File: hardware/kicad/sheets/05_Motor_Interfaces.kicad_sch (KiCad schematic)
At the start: 0 parts

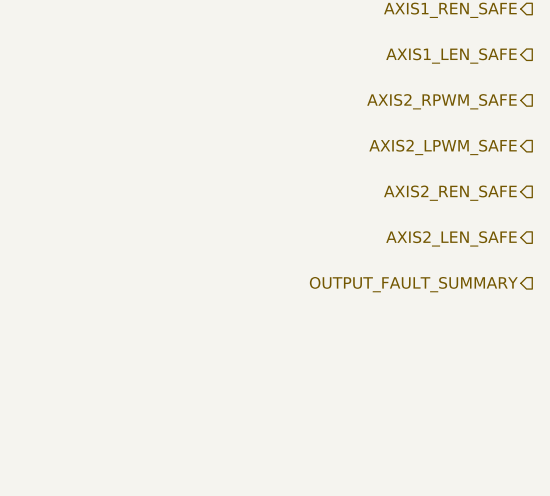
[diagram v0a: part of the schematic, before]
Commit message: Resolve Rev A motion interface contract
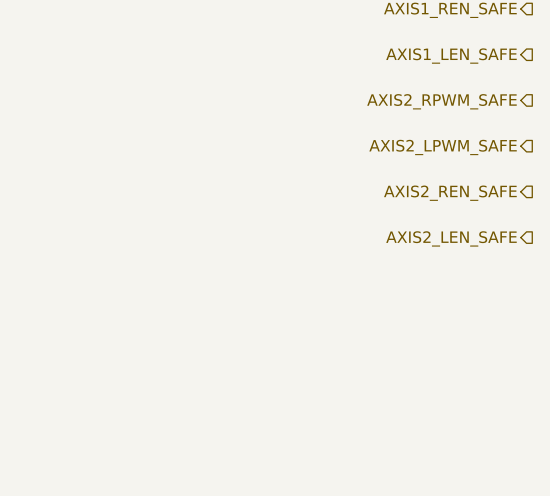
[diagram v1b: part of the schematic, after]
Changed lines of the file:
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@@
-    (effects (font (size 1.27 1.27)) (justify right))
-  )
-  (hierarchical_label "OUTPUT_FAULT_SUMMARY" (shape output) (at 180 85.64 180)
     (effects (font (size 1.27 1.27)) (justify right))
   )

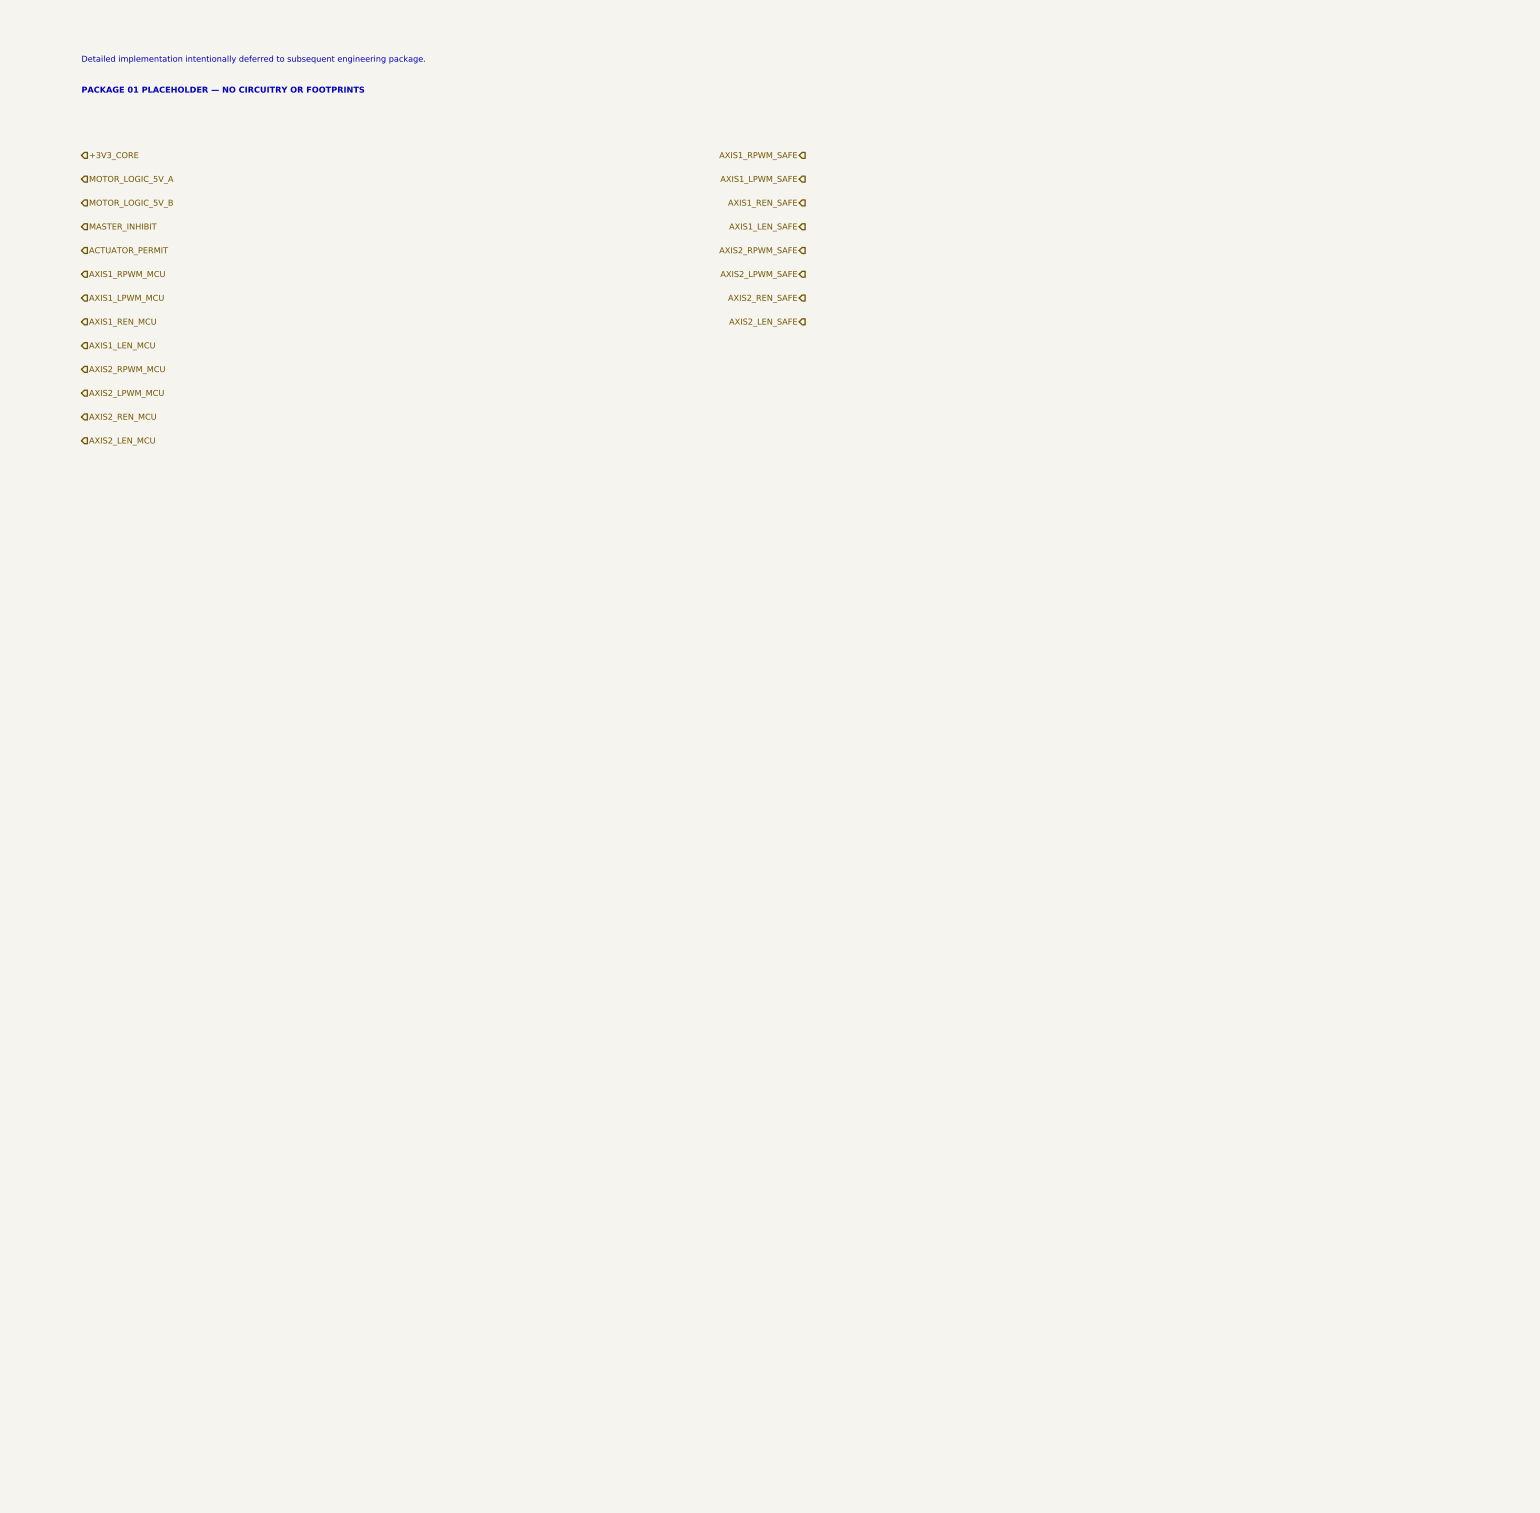
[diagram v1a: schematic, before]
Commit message: Implement dual-axis motion interface
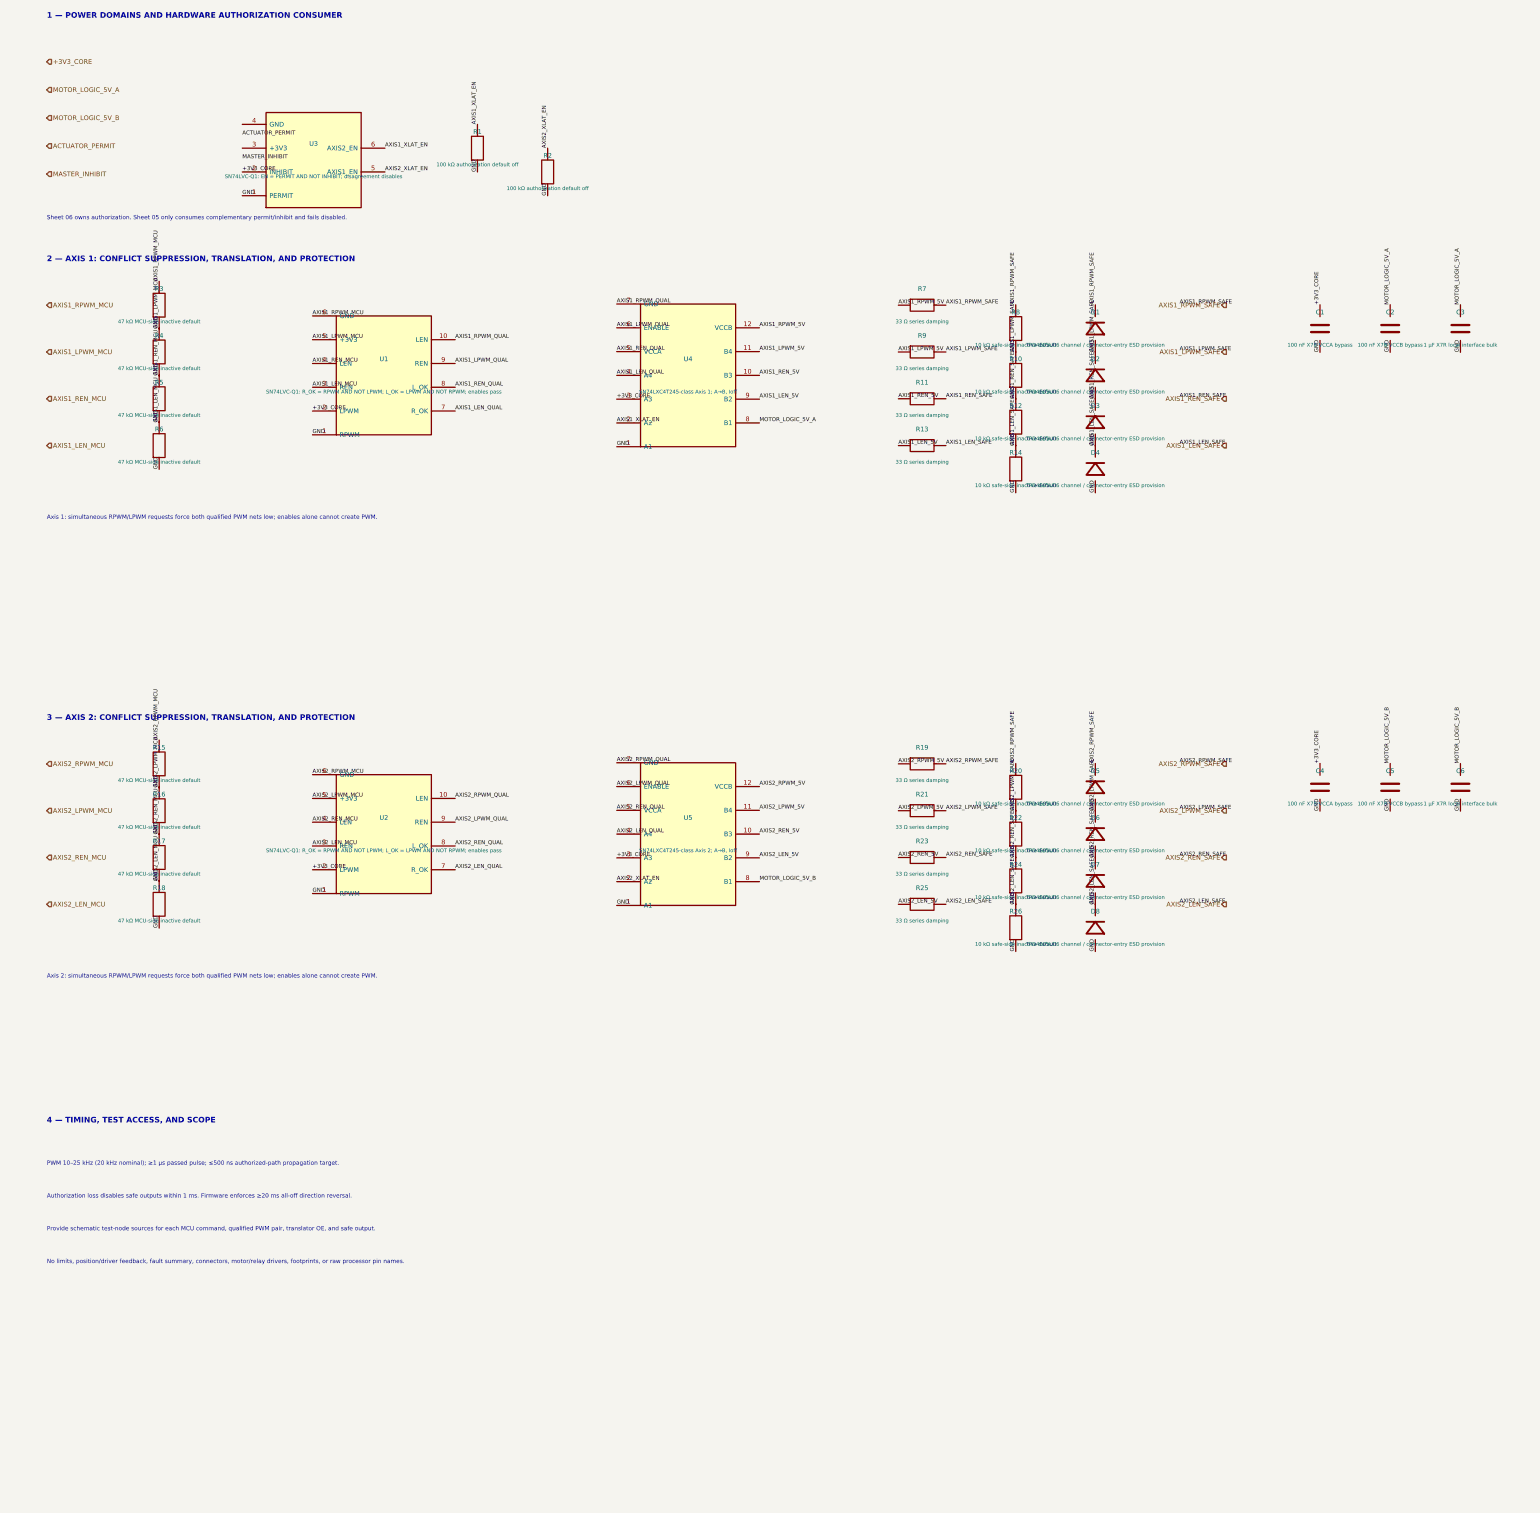
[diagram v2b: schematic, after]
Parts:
- added C1, C4: 100 nF X7R VCCA bypass, symbol IPC100:C
- added C2, C5: 100 nF X7R VCCB bypass, symbol IPC100:C
- added C3, C6: 1 µF X7R local interface bulk, symbol IPC100:C
- added D1, D2, D3, D4, D5, D6, D7, D8: TPD4E05U06 channel / connector-entry ESD provision, symbol IPC100:D
- added R1, R2: 100 kΩ authorization default off, symbol IPC100:R
- added R10, R12, R14, R20, R22, R24, R26, R8: 10 kΩ safe-side inactive default, symbol IPC100:R
- added R11, R13, R19, R21, R23, R25, R7, R9: 33 Ω series damping, symbol IPC100:R
- added R15, R16, R17, R18, R3, R4, R5, R6: 47 kΩ MCU-side inactive default, symbol IPC100:R
- added U1, U2: SN74LVC-Q1: R_OK = RPWM AND NOT LPWM; L_OK = LPWM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, symbol IPC100:INTERLOCK4
- added U3: SN74LVC-Q1: EN = PERMIT AND NOT INHIBIT; disagree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, symbol IPC100:AUTH2
- added U4: SN74LXC4T245-class Axis 1; A→B, Ioff, symbol IPC100:XLAT4
- added U5: SN74LXC4T245-class Axis 2; A→B, Ioff, symbol IPC100:XLAT4
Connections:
- net +3V3_CORE: now also C1.2, C4.2, U1.2 (LPWM), U2.2 (LPWM), U3.2 (INHIBIT), U4.3 (A3), U5.3 (A3)
- net AXIS1_LEN_MCU: now also R6.2, U1.3 (REN)
- net AXIS1_LEN_SAFE: now also D4.2, R13.2, R14.2
- net AXIS1_LPWM_MCU: now also R4.2, U1.5 (+3V3)
- net AXIS1_LPWM_SAFE: now also D2.2, R10.2, R9.2
- net AXIS1_REN_MCU: now also R5.2, U1.4 (LEN)
- net AXIS1_REN_SAFE: now also D3.2, R11.2, R12.2
- net AXIS1_RPWM_MCU: now also R3.2, U1.6 (GND)
- net AXIS1_RPWM_SAFE: now also D1.2, R7.2, R8.2
- net AXIS2_LEN_MCU: now also R18.2, U2.3 (REN)
- net AXIS2_LEN_SAFE: now also D8.2, R25.2, R26.2
- net AXIS2_LPWM_MCU: now also R16.2, U2.5 (+3V3)
- net AXIS2_LPWM_SAFE: now also D6.2, R21.2, R22.2
- net AXIS2_REN_MCU: now also R17.2, U2.4 (LEN)
- net AXIS2_REN_SAFE: now also D7.2, R23.2, R24.2
- net AXIS2_RPWM_MCU: now also R15.2, U2.6 (GND)
- net AXIS2_RPWM_SAFE: now also D5.2, R19.2, R20.2
- net MOTOR_LOGIC_5V_A: now also C2.2, C3.2, U4.8 (B1)
- net MOTOR_LOGIC_5V_B: now also C5.2, C6.2, U5.8 (B1)
- new net AXIS1_LEN_5V: R13.1, U4.9 (B2)
- new net AXIS1_LEN_QUAL: U1.7 (R_OK), U4.4 (A4)
- new net AXIS1_LPWM_5V: R9.1, U4.11 (B4)
- new net AXIS1_LPWM_QUAL: U1.9 (REN), U4.6 (ENABLE)
- new net AXIS1_REN_5V: R11.1, U4.10 (B3)
- new net AXIS1_REN_QUAL: U1.8 (L_OK), U4.5 (VCCA)
- new net AXIS1_RPWM_5V: R7.1, U4.12 (VCCB)
- new net AXIS1_RPWM_QUAL: U1.10 (LEN), U4.7 (GND)
- new net AXIS1_XLAT_EN: R1.2, U3.6 (AXIS2_EN), U4.2 (A2)
- new net AXIS2_LEN_5V: R25.1, U5.9 (B2)
- new net AXIS2_LEN_QUAL: U2.7 (R_OK), U5.4 (A4)
- new net AXIS2_LPWM_5V: R21.1, U5.11 (B4)
- new net AXIS2_LPWM_QUAL: U2.9 (REN), U5.6 (ENABLE)
- new net AXIS2_REN_5V: R23.1, U5.10 (B3)
- new net AXIS2_REN_QUAL: U2.8 (L_OK), U5.5 (VCCA)
- new net AXIS2_RPWM_5V: R19.1, U5.12 (VCCB)
- new net AXIS2_RPWM_QUAL: U2.10 (LEN), U5.7 (GND)
- new net AXIS2_XLAT_EN: R2.2, U3.5 (AXIS1_EN), U5.2 (A2)
- new net GND: C1.1, C2.1, C3.1, C4.1, C5.1, C6.1, D1.1, D2.1, D3.1, D4.1, D5.1, D6.1, D7.1, D8.1, R1.1, R10.1, R12.1, R14.1, R15.1, R16.1, R17.1, R18.1, R2.1, R20.1, R22.1, R24.1, R26.1, R3.1, R4.1, R5.1, R6.1, R8.1, U1.1 (RPWM), U2.1 (RPWM), U3.1 (PERMIT), U4.1 (A1), U5.1 (A1)
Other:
- note added: "1 — POWER DOMAINS AND HARDWARE AUTHORIZATION CONSUMER"
- note added: "2 — AXIS 1: CONFLICT SUPPRESSION, TRANSLATION, AND PROTECTION"
- note added: "3 — AXIS 2: CONFLICT SUPPRESSION, TRANSLATION, AND PROTECTION"
- note added: "4 — TIMING, TEST ACCESS, AND SCOPE"
- note added: "Authorization loss disables safe outputs within 1 ms. Firmware enforces ≥20 ms all-off direction reversal."
- note added: "Axis 1: simultaneous RPWM/LPWM requests force both qualified PWM nets low; enables alone cannot create PWM."
- note added: "Axis 2: simultaneous RPWM/LPWM requests force both qualified PWM nets low; enables alone cannot create PWM."
- note added: "No limits, position/driver feedback, fault summary, connectors, motor/relay drivers, footprints, or raw processor pin names."
- note added: "PWM 10–25 kHz (20 kHz nominal); ≥1 µs passed pulse; ≤500 ns authorized-path propagation target."
- note added: "Provide schematic test-node sources for each MCU command, qualified PWM pair, translator OE, and safe output."
- note added: "Sheet 06 owns authorization. Sheet 05 only consumes complementary permit/inhibit and fails disabled."
- note removed: "Detailed implementation intentionally deferred to subsequent engineering package."
- note removed: "PACKAGE 01 PLACEHOLDER — NO CIRCUITRY OR FOOTPRINTS"
- title: IPC-100 Rev A — 05 Motor Interfaces -> IPC-100 Rev A — 05 Axis Command Interface

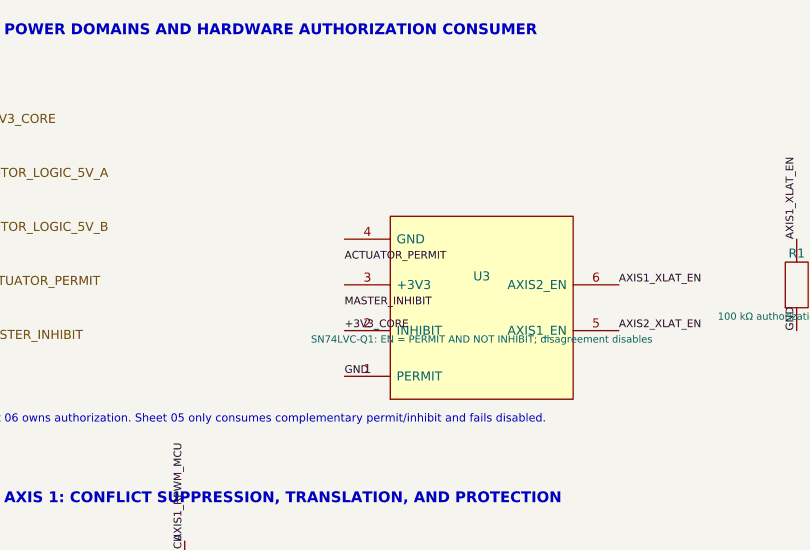
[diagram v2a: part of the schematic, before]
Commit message: Correct Sheet 05 authorization connectivity
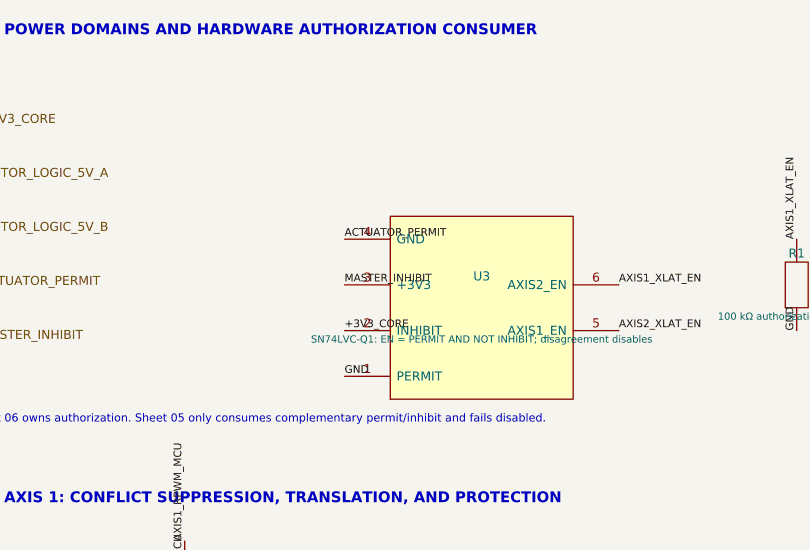
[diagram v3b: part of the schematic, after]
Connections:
- net ACTUATOR_PERMIT: now also U3.4 (GND)
- net MASTER_INHIBIT: now also U3.3 (+3V3)
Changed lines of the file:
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@@
     (instances (project "IPC-100" (path "/10000000-0000-4000-8000-000000000001/10000000-0000-4000-8000-000000000261" (reference "U3") (unit 1))))
   )
-  (label "ACTUATOR_PERMIT" (at 59.76 40.92 0) (effects (font (size 0.85 0.85)) (justify left bottom)))
-  (label "MASTER_INHIBIT" (at 59.76 46 0) (effects (font (size 0.85 0.85)) (justify left bottom)))
+  (label "ACTUATOR_PERMIT" (at 59.76 38.38 0) (effects (font (size 0.85 0.85)) (justify left bottom)))
+  (label "MASTER_INHIBIT" (at 59.76 43.46 0) (effects (font (size 0.85 0.85)) (justify left bottom)))
   (label "+3V3_CORE" (at 59.76 48.54 0) (effects (font (size 0.85 0.85)) (justify left bottom)))
   (label "GND" (at 59.76 53.62 0) (effects (font (size 0.85 0.85)) (justify left bottom)))

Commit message: Add deterministic authorization input bias
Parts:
- added R27: 100 kΩ U3 PERMIT fail-low input bias, symbol IPC100:R
- added R28: 100 kΩ U3 INHIBIT fail-high input bias, symbol IPC100:R
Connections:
- net +3V3_CORE: now also R28.2
- net ACTUATOR_PERMIT: now also R27.2
- net GND: now also R27.1
- net MASTER_INHIBIT: now also R28.1
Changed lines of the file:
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@@
   (label "AXIS2_XLAT_EN" (at 125 43.46 90) (effects (font (size 0.85 0.85)) (justify left bottom)))
   (label "GND" (at 125 53.62 90) (effects (font (size 0.85 0.85)) (justify left bottom)))
+  (symbol (lib_id "IPC100:R") (at 145 43.46 90) (unit 1) (exclude_from_sim no) (in_bom yes) (on_board yes) (dnp no)
+ (property "Reference" "R27" (at 145 39.96 90) (effects (font (size 1 1)))) (property "Value" "100 kΩ U3 PERMIT fail-low input bias" (at 145 46.96 90) (effects (font (size 0.8 0.8))))
+    (property "Footprint" "" (at 145 43.46 0) (effects (font (size 1 1)) hide)) (property "Datasheet" "" (at 145 43.46 0) (effects (font (size 1 1)) hide))
+    (pin "1")
+    (pin "2")
+    (instances (project "IPC-100" (path "/10000000-0000-4000-8000-000000000001/10000000-0000-4000-8000-000000000261" (reference "R27") (unit 1))))
+  )
+  (label "ACTUATOR_PERMIT" (at 145 38.38 90) (effects (font (size 0.85 0.85)) (justify left bottom)))
+  (label "GND" (at 145 48.54 90) (effects (font (size 0.85 0.85)) (justify left bottom)))
+  (symbol (lib_id "IPC100:R") (at 160 48.54 90) (unit 1) (exclude_from_sim no) (in_bom yes) (on_board yes) (dnp no)
+ (property "Reference" "R28" (at 160 45.04 90) (effects (font (size 1 1)))) (property "Value" "100 kΩ U3 INHIBIT fail-high input bias" (at 160 52.04 90) (effects (font (size 0.8 0.8))))
+    (property "Footprint" "" (at 160 48.54 0) (effects (font (size 1 1)) hide)) (property "Datasheet" "" (at 160 48.54 0) (effects (font (size 1 1)) hide))
+    (pin "1")
+    (pin "2")
+    (instances (project "IPC-100" (path "/10000000-0000-4000-8000-000000000001/10000000-0000-4000-8000-000000000261" (reference "R28") (unit 1))))
+  )
+  (label "+3V3_CORE" (at 160 43.46 90) (effects (font (size 0.85 0.85)) (justify left bottom)))
+  (label "MASTER_INHIBIT" (at 160 53.62 90) (effects (font (size 0.85 0.85)) (justify left bottom)))
   (text "Sheet 06 owns authorization. Sheet 05 only consumes complementary permit/inhibit and fails disabled." (at 18 59 0) (effects (font (size 0.9 0.9)) (justify left bottom)))
   (text "2 — AXIS 1: CONFLICT SUPPRESSION, TRANSLATION, AND PROTECTION" (at 18 68 0) (effects (font (size 1.2 1.2) (bold yes)) (justify left bottom)))
